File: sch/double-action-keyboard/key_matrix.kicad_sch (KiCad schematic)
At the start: 120 parts

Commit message: ダイオードの配置と配線を行いました。
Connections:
- net ROW4 is gone; now on net ROW2: SW21.3 (C0), SW22.3 (C0), SW23.3 (C0), SW24.3 (C0), SW25.3 (C0)
- net ROW5 is gone; now on net ROW2: SW26.3 (C0), SW27.3 (C0), SW28.3 (C0), SW29.3 (C0), SW30.3 (C0)
- net ROW6 is gone; now on net ROW3: SW31.3 (C0), SW32.3 (C0), SW33.3 (C0), SW34.3 (C0), SW35.3 (C0)
- net ROW7 is gone; now on net ROW3: SW36.3 (C0), SW37.3 (C0), SW38.3 (C0), SW39.3 (C0), SW40.3 (C0)
- net COL0: no longer D11.2 (A), D31.2 (A), D51.2 (A), D71.2 (A)
- net COL1: no longer D12.2 (A), D32.2 (A), D52.2 (A), D72.2 (A)
- net COL2: no longer D13.2 (A), D33.2 (A), D53.2 (A), D73.2 (A)
- net COL3: no longer D14.2 (A), D34.2 (A), D54.2 (A), D74.2 (A)
- net COL4: no longer D15.2 (A), D35.2 (A), D55.2 (A), D75.2 (A)
- net COL5: no longer D16.2 (A), D36.2 (A), D56.2 (A), D76.2 (A)
- net COL6: no longer D17.2 (A), D37.2 (A), D57.2 (A), D77.2 (A)
- net COL7: no longer D18.2 (A), D38.2 (A), D58.2 (A), D78.2 (A)
- net COL8: no longer D19.2 (A), D39.2 (A), D59.2 (A), D79.2 (A)
- net COL9: no longer D20.2 (A), D40.2 (A), D60.2 (A), D80.2 (A)
- net ROW0: now also SW10.3 (C0), SW6.3 (C0), SW7.3 (C0), SW8.3 (C0), SW9.3 (C0)
- net ROW1: now also SW11.3 (C0), SW12.3 (C0), SW13.3 (C0), SW14.3 (C0), SW15.3 (C0), SW16.3 (C0), SW17.3 (C0), SW18.3 (C0), SW19.3 (C0), SW20.3 (C0); no longer SW10.3 (C0), SW6.3 (C0), SW7.3 (C0), SW8.3 (C0), SW9.3 (C0)
- net ROW2: no longer SW11.3 (C0), SW12.3 (C0), SW13.3 (C0), SW14.3 (C0), SW15.3 (C0)
- net ROW3: no longer SW16.3 (C0), SW17.3 (C0), SW18.3 (C0), SW19.3 (C0), SW20.3 (C0)
- new net COL10: D11.2 (A), D31.2 (A), D51.2 (A), D71.2 (A)
- new net COL11: D12.2 (A), D32.2 (A), D52.2 (A), D72.2 (A)
- new net COL12: D13.2 (A), D33.2 (A), D53.2 (A), D73.2 (A)
- new net COL13: D14.2 (A), D34.2 (A), D54.2 (A), D74.2 (A)
- new net COL14: D15.2 (A), D35.2 (A), D55.2 (A), D75.2 (A)
- new net COL15: D16.2 (A), D36.2 (A), D56.2 (A), D76.2 (A)
- new net COL16: D17.2 (A), D37.2 (A), D57.2 (A), D77.2 (A)
- new net COL17: D18.2 (A), D38.2 (A), D58.2 (A), D78.2 (A)
- new net COL18: D19.2 (A), D39.2 (A), D59.2 (A), D79.2 (A)
- new net COL19: D20.2 (A), D40.2 (A), D60.2 (A), D80.2 (A)

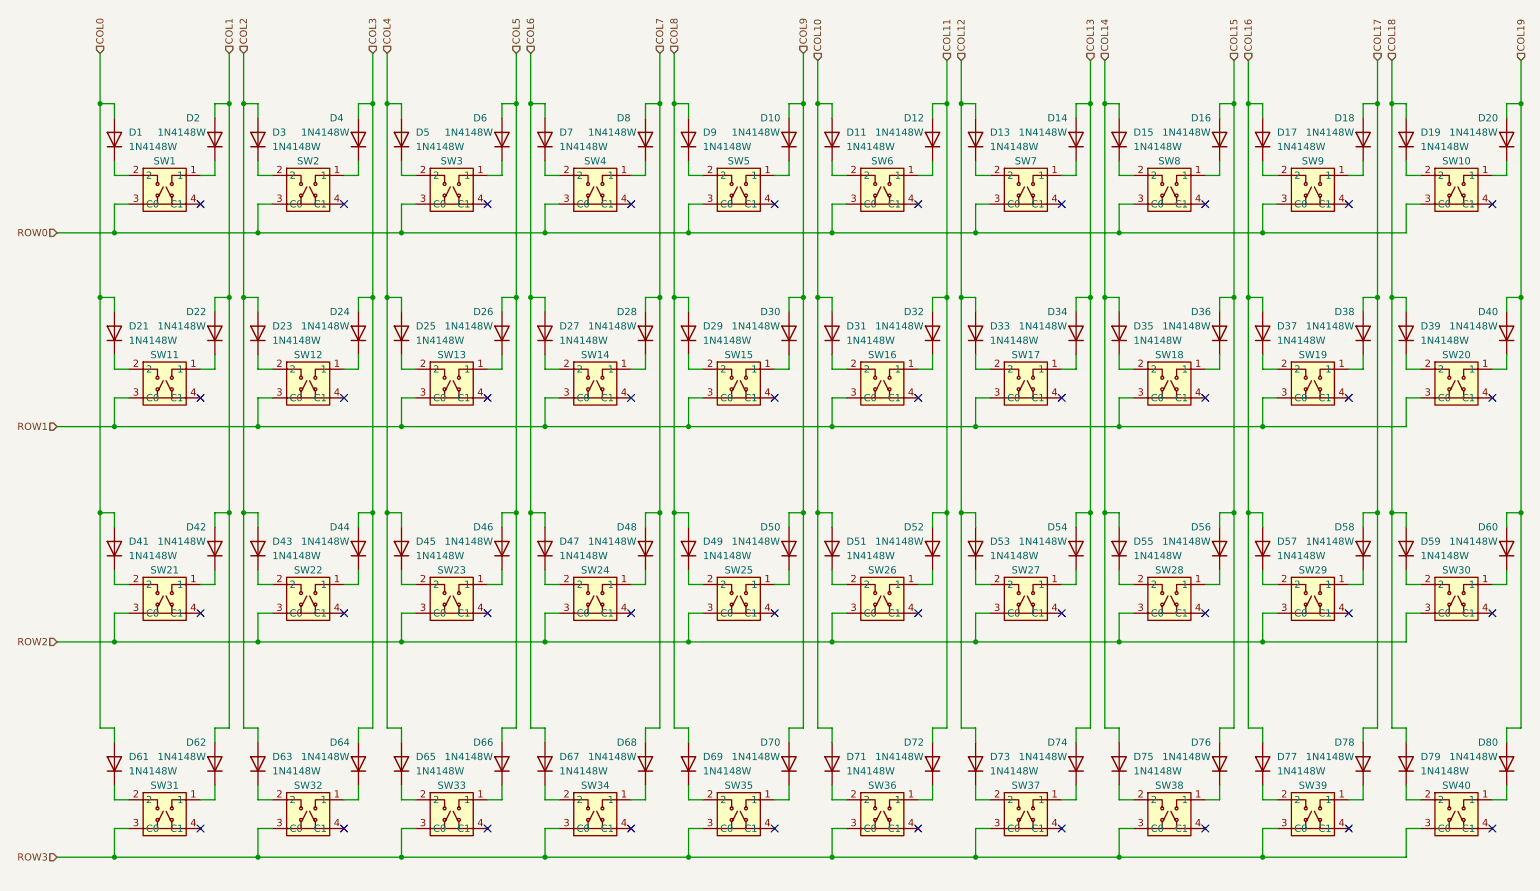
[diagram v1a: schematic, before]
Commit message: KiCad 8.0にアップデートしました。 部品配置をやり直し中。
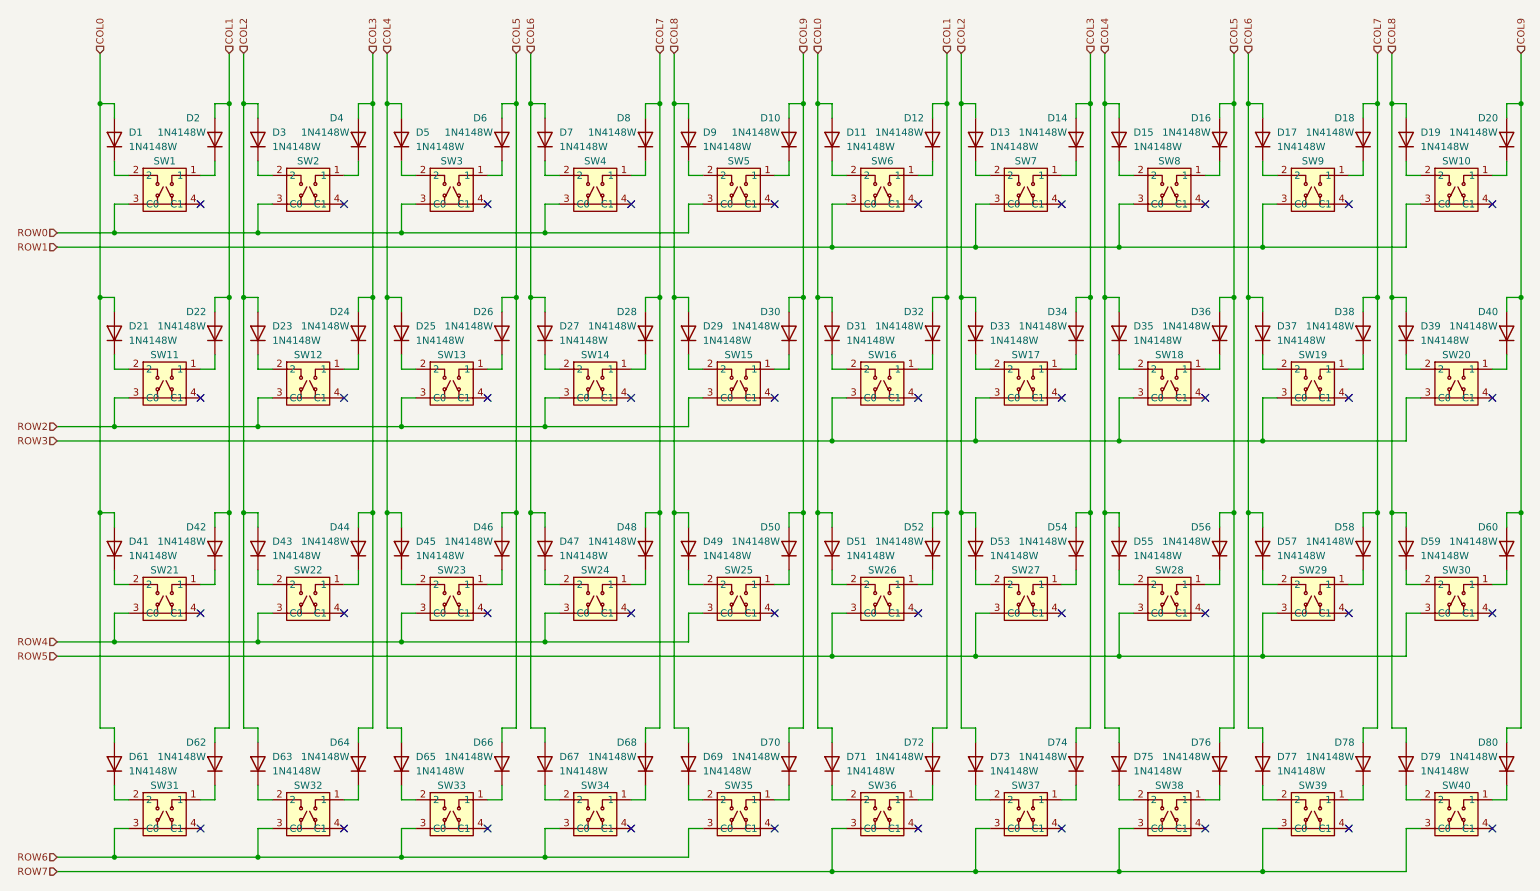
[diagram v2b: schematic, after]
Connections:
- net COL10 is gone; now on net COL0: D11.2 (A), D31.2 (A), D51.2 (A), D71.2 (A)
- net COL11 is gone; now on net COL1: D12.2 (A), D32.2 (A), D52.2 (A), D72.2 (A)
- net COL12 is gone; now on net COL2: D13.2 (A), D33.2 (A), D53.2 (A), D73.2 (A)
- net COL13 is gone; now on net COL3: D14.2 (A), D34.2 (A), D54.2 (A), D74.2 (A)
- net COL14 is gone; now on net COL4: D15.2 (A), D35.2 (A), D55.2 (A), D75.2 (A)
- net COL15 is gone; now on net COL5: D16.2 (A), D36.2 (A), D56.2 (A), D76.2 (A)
- net COL16 is gone; now on net COL6: D17.2 (A), D37.2 (A), D57.2 (A), D77.2 (A)
- net COL17 is gone; now on net COL7: D18.2 (A), D38.2 (A), D58.2 (A), D78.2 (A)
- net COL18 is gone; now on net COL8: D19.2 (A), D39.2 (A), D59.2 (A), D79.2 (A)
- net COL19 is gone; now on net COL9: D20.2 (A), D40.2 (A), D60.2 (A), D80.2 (A)
- net ROW0: no longer SW10.3 (C0), SW6.3 (C0), SW7.3 (C0), SW8.3 (C0), SW9.3 (C0)
- net ROW1: now also SW10.3 (C0), SW6.3 (C0), SW7.3 (C0), SW8.3 (C0), SW9.3 (C0); no longer SW11.3 (C0), SW12.3 (C0), SW13.3 (C0), SW14.3 (C0), SW15.3 (C0), SW16.3 (C0), SW17.3 (C0), SW18.3 (C0), SW19.3 (C0), SW20.3 (C0)
- net ROW2: now also SW11.3 (C0), SW12.3 (C0), SW13.3 (C0), SW14.3 (C0), SW15.3 (C0); no longer SW21.3 (C0), SW22.3 (C0), SW23.3 (C0), SW24.3 (C0), SW25.3 (C0), SW26.3 (C0), SW27.3 (C0), SW28.3 (C0), SW29.3 (C0), SW30.3 (C0)
- net ROW3: now also SW16.3 (C0), SW17.3 (C0), SW18.3 (C0), SW19.3 (C0), SW20.3 (C0); no longer SW31.3 (C0), SW32.3 (C0), SW33.3 (C0), SW34.3 (C0), SW35.3 (C0), SW36.3 (C0), SW37.3 (C0), SW38.3 (C0), SW39.3 (C0), SW40.3 (C0)
- new net ROW4: SW21.3 (C0), SW22.3 (C0), SW23.3 (C0), SW24.3 (C0), SW25.3 (C0)
- new net ROW5: SW26.3 (C0), SW27.3 (C0), SW28.3 (C0), SW29.3 (C0), SW30.3 (C0)
- new net ROW6: SW31.3 (C0), SW32.3 (C0), SW33.3 (C0), SW34.3 (C0), SW35.3 (C0)
- new net ROW7: SW36.3 (C0), SW37.3 (C0), SW38.3 (C0), SW39.3 (C0), SW40.3 (C0)
